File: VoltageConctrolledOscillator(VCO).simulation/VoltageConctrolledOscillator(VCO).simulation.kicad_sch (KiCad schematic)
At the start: 0 parts

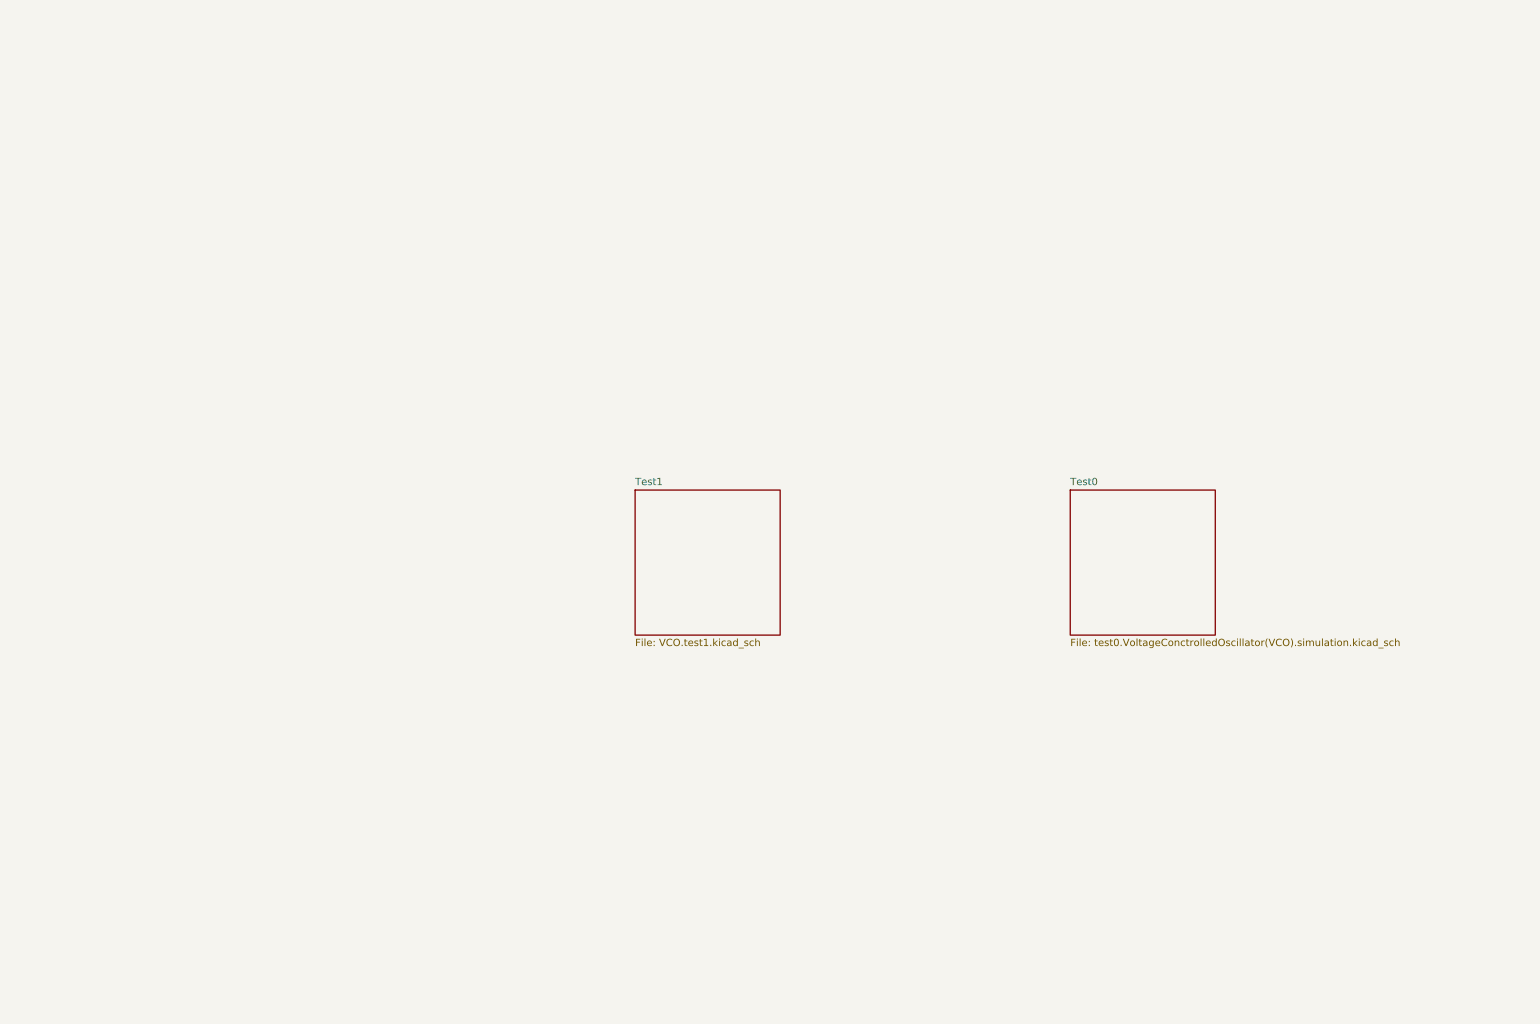
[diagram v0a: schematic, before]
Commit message: Rearrange sheets
Move stuff around sheets for future project evolution :
* Voltage sources are moved on top hierarchical page
* Hierarchical label is used to set input voltage to Test 1 sheet
* Add text on Test 0 sheet
* All subsheet page are A5 size for ease of read reason.
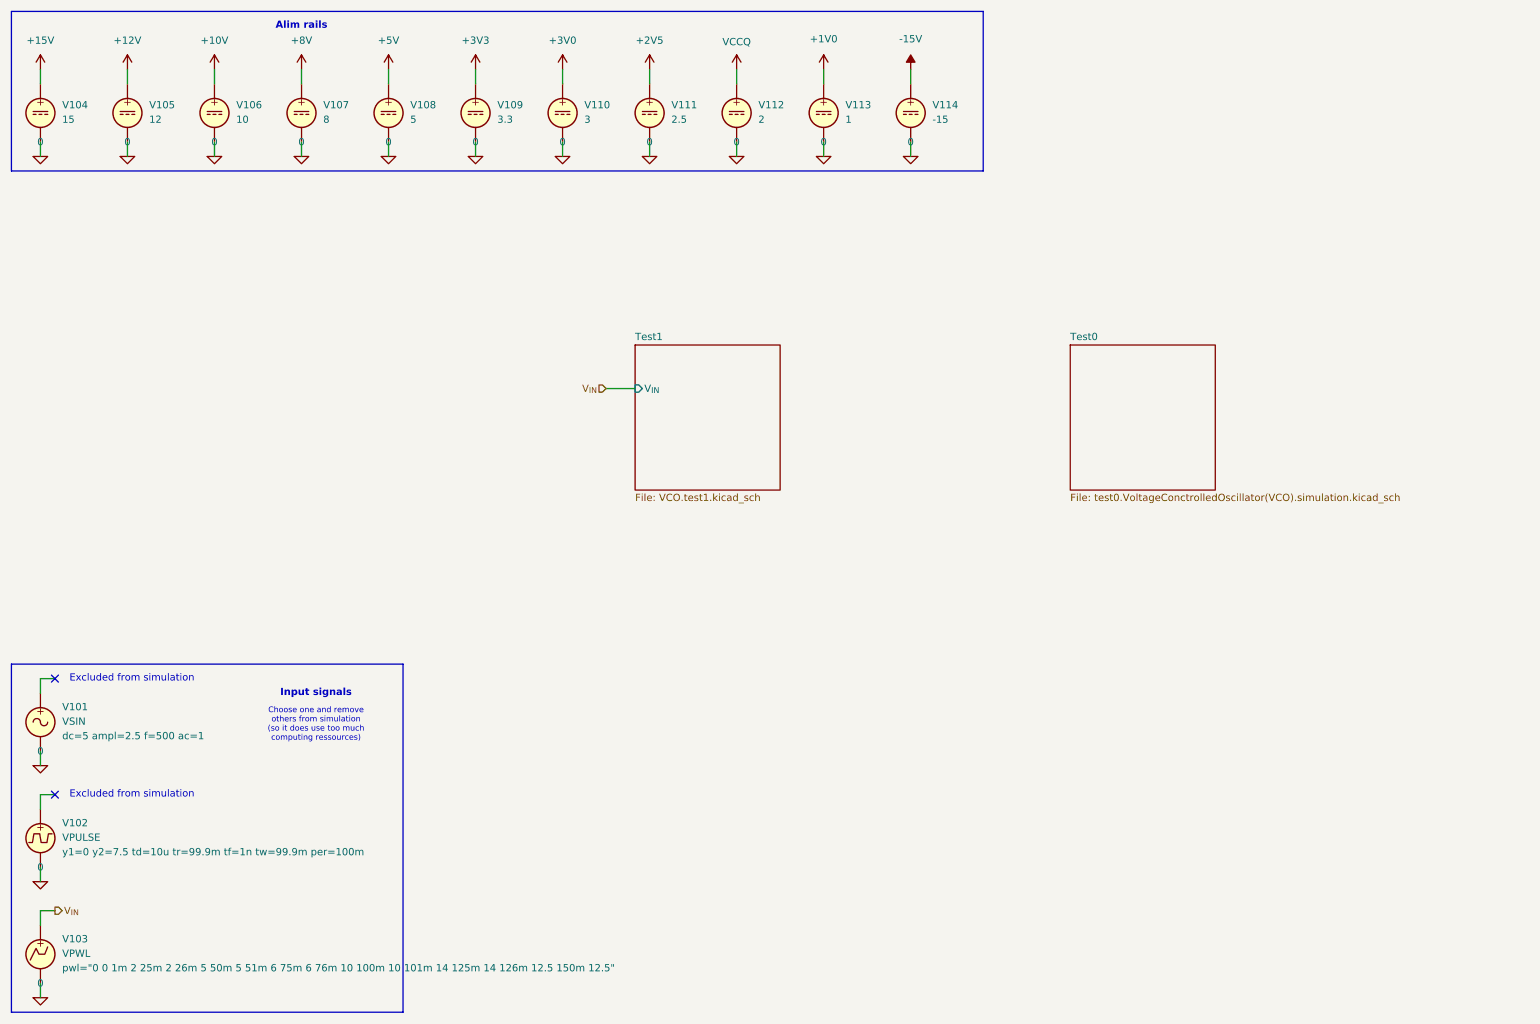
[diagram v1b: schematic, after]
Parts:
- added V101: VSIN, symbol Simulation_SPICE:VSIN
- added V102: VPULSE, symbol Simulation_SPICE:VPULSE
- added V103: VPWL, symbol Simulation_SPICE:VPWL
- added V104: 15, symbol Simulation_SPICE:VDC
- added V105: 12, symbol Simulation_SPICE:VDC
- added V106: 10, symbol Simulation_SPICE:VDC
- added V107: 8, symbol Simulation_SPICE:VDC
- added V108: 5, symbol Simulation_SPICE:VDC
- added V109: 3.3, symbol Simulation_SPICE:VDC
- added V110: 3, symbol Simulation_SPICE:VDC
- added V111: 2.5, symbol Simulation_SPICE:VDC
- added V112: 2, symbol Simulation_SPICE:VDC
- added V113: 1, symbol Simulation_SPICE:VDC
- added V114: -15, symbol Simulation_SPICE:VDC
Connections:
- new net +10V: V106.1
- new net +12V: V105.1
- new net +15V: V104.1
- new net +1V0: V113.1
- new net +2V5: V111.1
- new net +3V0: V110.1
- new net +3V3: V109.1
- new net +5V: V108.1
- new net +8V: V107.1
- new net -15V: V114.1
- new net 0: V101.2, V102.2, V103.2, V104.2, V105.2, V106.2, V107.2, V108.2, V109.2, V110.2, V111.2, V112.2, V113.2, V114.2
- new net VCCQ: V112.1
- new net V_{IN}: V103.1
- no-connect marks 0 -> 2
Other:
- sheet Test1 ports: added V_{IN}; removed none
- note added: "Alim rails"
- note added: "Choose one and remove others from simulation (so it does use too much computing ressources)"
- note added: "Excluded from simulation"
- note added: "Input signals"

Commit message: [WIP] Implement VCO from onsemi datasheet
Try to implement VCO function block from _onsemi_ 's
FAN7621B component datasheet.
/!\/!\/!\ Component is OBSOLETE /!\/!\/!\
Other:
- added sheet Test 2 (VCO.test2.kicad_sch)
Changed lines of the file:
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@@
+		)
+	)
+	(sheet
+		(at 50.8 76.2)
+		(size 25.4 25.4)
+		(fields_autoplaced yes)
+		(stroke
+			(width 0.1524)
+			(type solid)
+		)
+		(fill
+			(color 0 0 0 0.0000)
+		)
+		(property "Sheetname" "Test 2"
+			(at 50.8 75.4884 0)
+			(effects
+				(font
+					(size 1.27 1.27)
+				)
+				(justify left bottom)
+			)
+		)
+		(property "Sheetfile" "VCO.test2.kicad_sch"
+			(at 50.8 102.1846 0)
+			(effects
+				(font
+					(size 1.27 1.27)
+				)
+				(justify left top)
+			)
+		)
+		(instances
+			(project "VoltageConctrolledOscillator(VCO).simulation"
+				(path "/39e238e2-77a8-4917-9f90-31fbe07c1d9b"
+					(page "4")
+				)
+			)
 		)
 	)
